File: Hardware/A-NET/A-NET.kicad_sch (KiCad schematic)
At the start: 0 parts

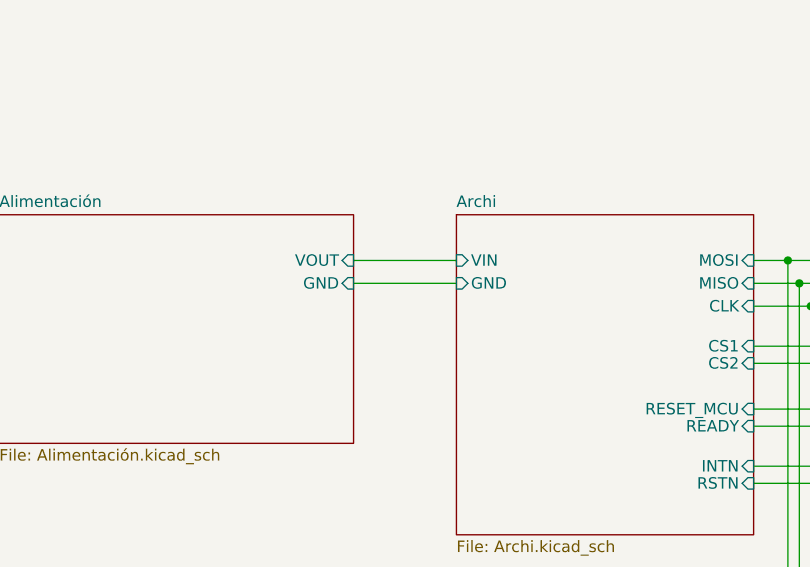
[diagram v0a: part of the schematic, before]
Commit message: add digikey | add POE
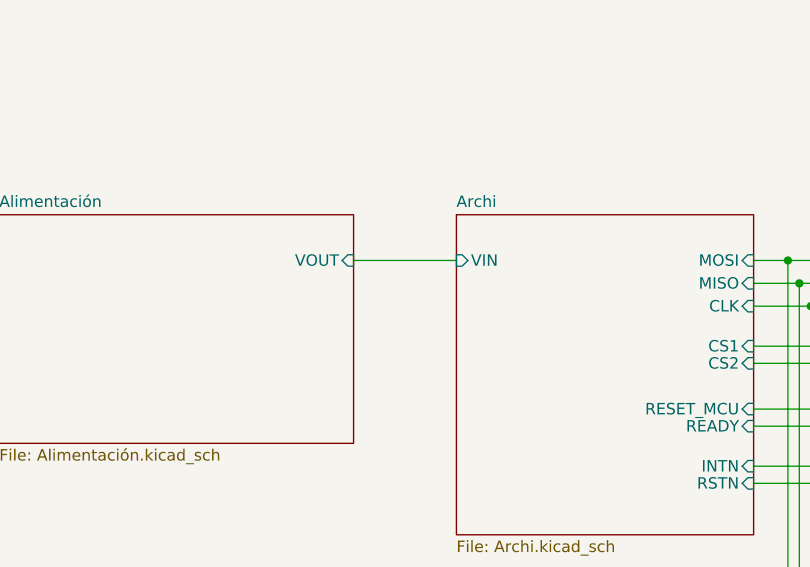
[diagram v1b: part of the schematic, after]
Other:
- sheet Alimentación ports: added none; removed GND
- sheet Archi ports: added none; removed GND
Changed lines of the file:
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@@
-	(wire
-		(pts
-			(xy 116.84 66.04) (xy 128.27 66.04)
-		)
-		(stroke
-			(width 0)
-			(type default)
-		)
-	)
 	(wire
 		(pts
@@
 			)
 		)
-		(pin "GND" input
-			(at 128.27 66.04 180)
-			(effects
-				(font
-					(size 1.27 1.27)
-				)
-				(justify left)
-			)
-		)
 		(pin "INTN" input
 			(at 161.29 86.36 0)
@@
 			)
 		)
-		(pin "GND" input
-			(at 116.84 66.04 0)
-			(effects
-				(font
-					(size 1.27 1.27)
-				)
-				(justify right)
-			)
-		)
